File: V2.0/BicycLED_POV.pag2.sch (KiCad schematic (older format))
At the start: 136 parts, among them U10 74x595, U11 74x595, U12 74x595, U13 74x595, U14 74x595, U7 74x595, U8 74x595, U9 74x595

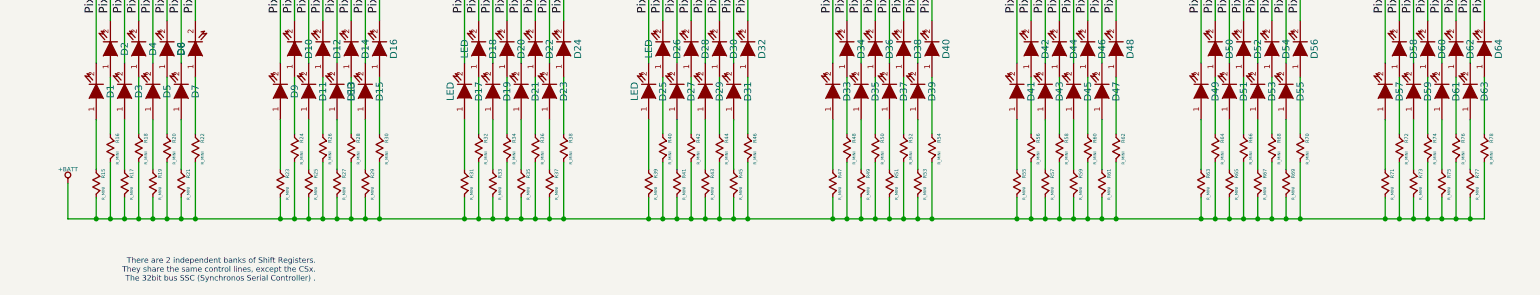
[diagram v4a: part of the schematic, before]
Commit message: 
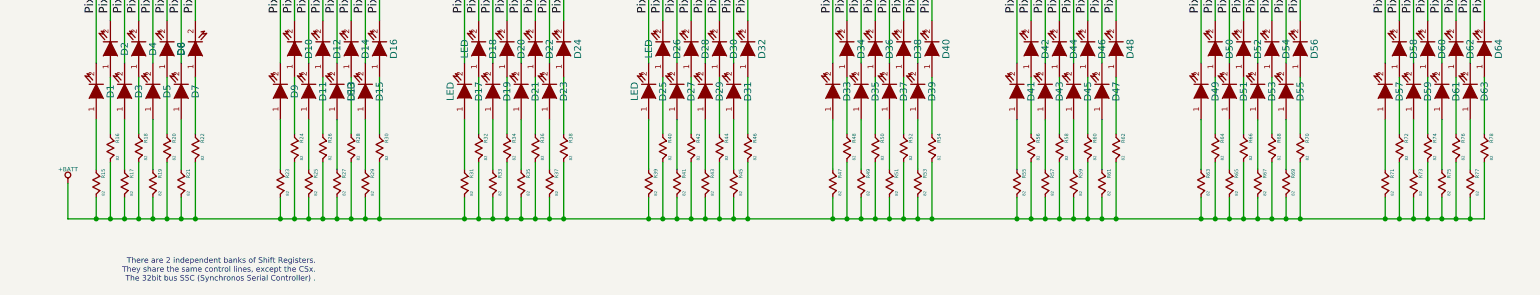
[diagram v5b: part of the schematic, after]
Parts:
- R15, R16, R17, R18, R19, R20, R21, R22, R23, R24, R25, R26, R27, R28, R29, R30, R31, R32, R33, R34, R35, R36, R37, R38, R39, R40, R41, R42, R43, R44, R45, R46, R47, R48, R49, R50, R51, R52, R53, R54, R55, R56, R57, R58, R59, R60, R61, R62, R63, R64, R65, R66, R67, R68, R69, R70, R71, R72, R73, R74, R75, R76, R77, R78: value R_MINI -> 82

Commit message: brd: created
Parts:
- R15, R16, R17, R18, R19, R20, R21, R22, R23, R24, R25, R26, R27, R28, R29, R30, R31, R32, R33, R34, R35, R36, R37, R38, R39, R40, R41, R42, R43, R44, R45, R46, R47, R48, R49, R50, R51, R52, R53, R54, R55, R56, R57, R58, R59, R60, R61, R62, R63, R64, R65, R66, R67, R68, R69, R70, R71, R72, R73, R74, R75, R76, R77, R78: value 82 -> 82R
